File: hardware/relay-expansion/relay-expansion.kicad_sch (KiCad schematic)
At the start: 12 parts

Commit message: Diseños casi listos (sch)
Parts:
- removed J?: (no value), symbol Connector_Generic:Conn_02x05_Odd_Even
- removed SW?: SW_DIP_x03, symbol Switch:SW_DIP_x03
- added J?: Conn_02x06_Odd_Even, Connector_PinHeader_2.54mm:PinHeader_2x06_P2.54mm_Vertical, symbol Connector_Generic:Conn_02x06_Odd_Even
- added JP? (x3): SolderJumper_2_Open, symbol Jumper:SolderJumper_2_Open
- J?: value Conn_01x03 -> (none)
- J?: value Conn_01x10 -> (none)
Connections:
- net +12V: now also J?.1 (Pin_1)
- net +3V3: now also J?.2 (Pin_2), JP?.1 (A), JP?.1 (A), JP?.1 (A)
- net GND: now also J?.12 (Pin_12), J?.3 (Pin_3)
- net at R?.1, U?.2 (A1): now also JP?.2 (B)
- net at R?.1, U?.1 (A0): now also JP?.2 (B)
- net at J?.7 (Pin_7), U?.10 (P5): now also J?.9 (Pin_9)
- net at J?.8 (Pin_8), U?.11 (P6): now also J?.10 (Pin_10)
- net at J?.9 (Pin_9), U?.12 (P7): now also J?.11 (Pin_11)
- net at R?.1, U?.3 (A2): now also JP?.2 (B)
- net at J?.2 (Pin_2), U?.4 (P0): now also J?.4 (Pin_4)
- net at J?.3 (Pin_3), U?.5 (P1): now also J?.5 (Pin_5)
- net at J?.4 (Pin_4), U?.6 (P2): now also J?.6 (Pin_6)
- net at J?.5 (Pin_5), U?.7 (P3): now also J?.7 (Pin_7)
- net at J?.6 (Pin_6), U?.9 (P4): now also J?.8 (Pin_8)

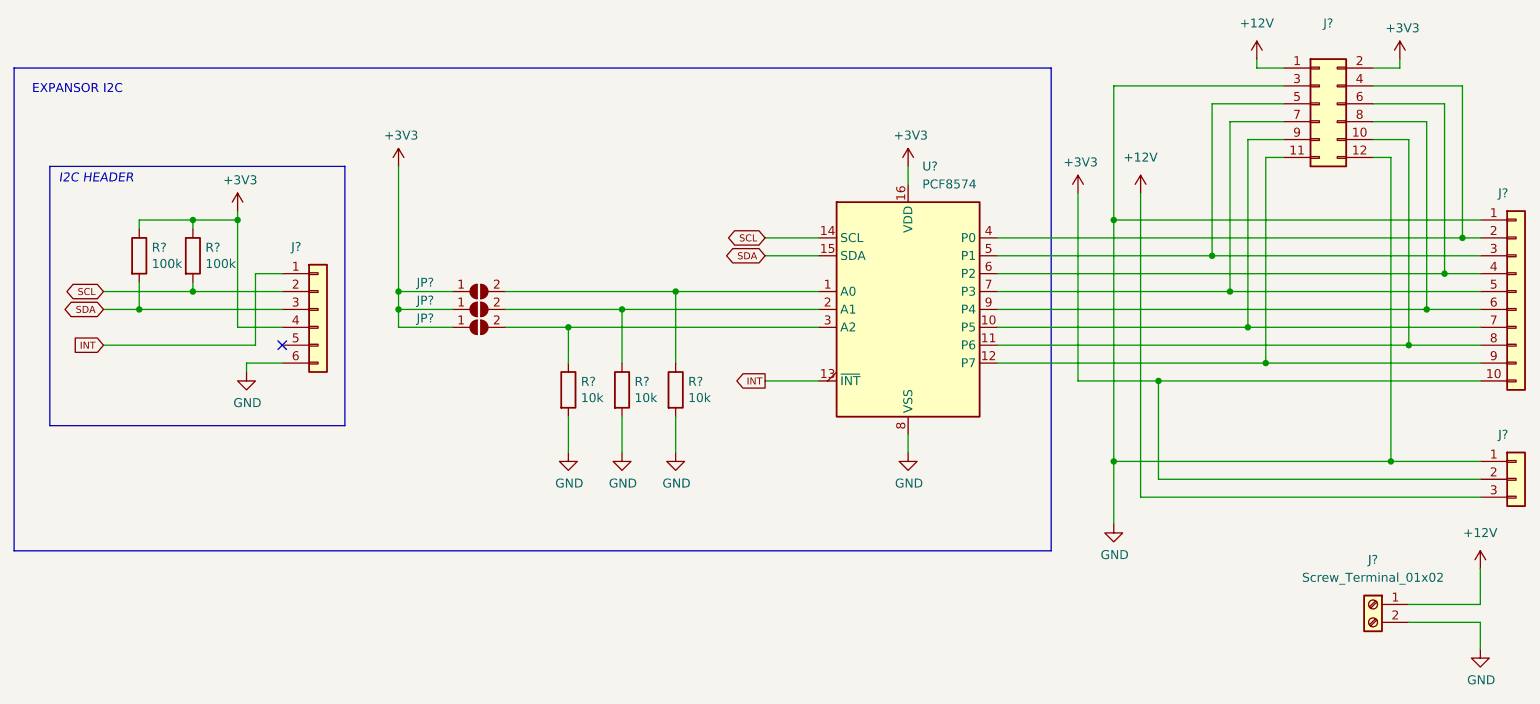
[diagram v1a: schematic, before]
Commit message: PCB Design for relay-expansion board done, added mechanical 3d files (solidworks 2016)
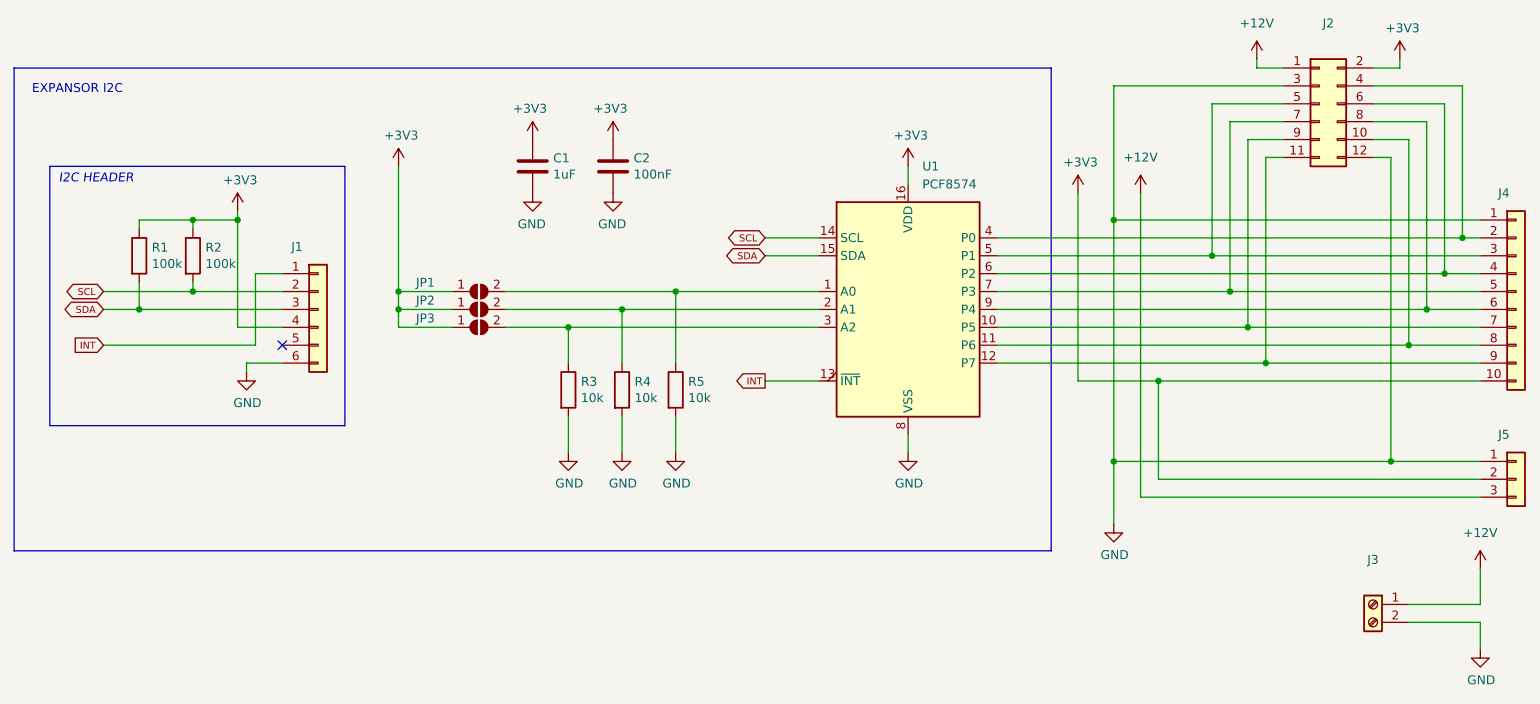
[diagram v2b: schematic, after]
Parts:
- added C1: 1uF, Capacitor_SMD:C_1206_3216Metric_Pad1.33x1.80mm_HandSolder, symbol Device:C
- added C2: 100nF, Capacitor_SMD:C_1206_3216Metric_Pad1.33x1.80mm_HandSolder, symbol Device:C
- J3: renamed from J?; value Screw_Terminal_01x02 -> (none)
- J4: renamed from J?; value (none) -> Conn_01x10; footprint (none) -> Connector_PinSocket_2.54mm:PinSocket_1x10_P2.54mm_Vertical
- J5: renamed from J?; value (none) -> Conn_01x03; footprint (none) -> Connector_PinSocket_2.54mm:PinSocket_1x03_P2.54mm_Vertical
- JP1, JP2, JP3: renamed from JP?; footprint (none) -> Jumper:SolderJumper-2_P1.3mm_Open_RoundedPad1.0x1.5mm
- gave numbers to parts that had none: 8
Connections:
- net +3V3: now also C1.1, C2.1
- net GND: now also C1.2, C2.2
